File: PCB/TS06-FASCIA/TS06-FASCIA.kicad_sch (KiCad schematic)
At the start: 0 parts

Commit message: Add TS06 symbol library and the TS06-FASCIA schematic
tools/mksch.py generates both. 14 parts: SW1 rotary, SW2/SW3 levers, SW4/SW5
buttons, R1-R5 (4.7k 1% A6 divider), R6-R8 (A7 lever ladder), J1 6-pin JST-XH.
Balanced-parens checked; nets verified by label count.

No power symbols. This board has no power source - every net leaves through J1 -
so +5V and GND are plain local labels. A power flag here would describe nothing.

The rotary symbol's six taps are pitched 12.7mm so they sit directly opposite
their ladder nodes and the divider reads as the physical thing it is, top to
bottom, 0V to 5V.

Sheet carries four notes so the reasoning survives without the spec open: the two
ADC tables, why the 100nF caps are deliberately NOT here (they belong at the main
board end), and the lug geometry that rules out board-mounting anything.

Project sym-lib-table and fp-lib-table registered so TS06: resolves on open.

Co-Authored-By: Claude Opus 5 <noreply@anthropic.com>
Claude-Session: https://claude.ai/code/session_01Wbajb7CU1SV8ZUPn3KkB8i
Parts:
- added J1: JST-XH 6, symbol TS06:Conn_JST_XH_6
- added R1, R2, R3, R4, R5: 4.7k 1%, symbol TS06:R
- added R6, R8: 10k, symbol TS06:R
- added R7: 20k, symbol TS06:R
- added SW1: SR25 6-pos, symbol TS06:SW_Rotary_6P1W
- added SW2: LEVER A, symbol TS06:SW_Lever_MT1
- added SW3: LEVER B, symbol TS06:SW_Lever_MT1
- added SW4: MINUS, symbol TS06:SW_Button_KMD1
- added SW5: PLUS, symbol TS06:SW_Button_KMD1
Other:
- note added: "A6: five 4.7k 1% across +5V/GND, wiper picks a node. 23.5k string, 213uA, worst source Z 5.64k (ADC wants <10k). Taps land on 0/1/2/3/4/5 V -> ADC 0/205/409/614/818/1023, worst gap 204 codes."
- note added: "A7: 10k pull-up, 20k and 10k to ground. Four states at ADC 1023 / 682 / 512 / 409, worst gap 103 codes."
- note added: "Every switch is panel-mount with solder lugs sitting >=11.3mm BEHIND this board, pointing away. Nothing here is board-mounted; all are hand-wired to landing pads. Pole 2 of the rotary is spare and unwired."
- note added: "Five controls, six wires. The ladder is why."
- note added: "NOT on this board: the two 100nF filter caps. They go at the MAIN BOARD end of the cable, where they hold the last value if a non-shorting wiper floats and filter what the cable picks up passing a converter switching 185V at 31kHz."
- note added: "TS06-FASCIA - control panel and product face"

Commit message: Control scheme rev B: swap INFO to position 6, give SUB the glitch rate
Two changes to spec section 1, decided while designing the fascia face. Spec section
1 is not yet rewritten - this file is the authority until the sweep runs.

INFO and FORMAT/DATE swap. Section 1 already called positions 1 and 5 the two screens
that ignore every input; rev A left one of them mid-arc. Rev B puts both parking
screens on end stops, so the knob cannot be knocked past either end into a live
editing screen. Costs one row of the A6 threshold table - the voltages do not move,
only the screen each maps to.

SUB gains the glitch rate on Display, read only while FIELD = Effects. The point is
not the feature but that SUB now obeys a rule instead of an exception: it is read
only when FIELD is thrown to its second position, true on both screens that use it.
A rule can be learned once; an exception has to be printed.

Co-Authored-By: Claude Opus 5 <noreply@anthropic.com>
Claude-Session: https://claude.ai/code/session_01Wbajb7CU1SV8ZUPn3KkB8i
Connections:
- net +5V: now also J1.2 (+5V), R5.1, R6.1, SW1.6 (T6)
- net A6: now also J1.3 (A6), SW1.7 (COM)
- net A7: now also J1.4 (A7), R6.2, SW2.2 (B), SW3.2 (B)
- net D7: now also J1.5 (D7), SW4.2
- net D8: now also J1.6 (D8), SW5.2
- net GND: now also J1.1 (GND), R1.2, R7.2, R8.2, SW1.1 (T1), SW4.1, SW5.1
- new net: R8.1, SW3.1 (A)
- new net: R7.1, SW2.1 (A)
- new net: R1.1, R2.2, SW1.2 (T2)
- new net: R2.1, R3.2, SW1.3 (T3)
- new net: R3.1, R4.2, SW1.4 (T4)
- new net: R4.1, R5.2, SW1.5 (T5)
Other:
- company: (none) -> TERMINAL-06
- title: (none) -> TS06-FASCIA - control panel and product face
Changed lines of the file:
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@@
 (generator_version "10.0")
 (paper "A4")
+(title_block
+(title "TS06-FASCIA - control panel and product face")
+(date "2026-09-08")
+(rev "A")
+(company "TERMINAL-06")
+(comment 1 "Five controls, six wires. Generated by tools/mksch.py")
+(comment 2 "Dimensions from the calipered FreeCAD models in 3d/")
+)
 (symbol
 (lib_id "TS06:SW_Rotary_6P1W")
@@
 (pts
 (xy 139.7 107.95)
-(xy 139.7 114.3)
-)
-(stroke
-(width 0)
-(type default)
-)
-)
-(wire
-(pts
-(xy 139.7 121.92)
+(xy 139.7 110.49)
+)
+(stroke
+(width 0)
+(type default)
+)
+)
+(wire
+(pts
+(xy 139.7 125.73)
 (xy 139.7 127.0)
 )
@@
 (pts
 (xy 165.1 107.95)
-(xy 165.1 114.3)
-)
-(stroke
-(width 0)
-(type default)
-)
-)
-(wire
-(pts
-(xy 165.1 121.92)
+(xy 165.1 110.49)
+)
+(stroke
+(width 0)
+(type default)
+)
+)
+(wire
+(pts
+(xy 165.1 125.73)
 (xy 165.1 127.0)
 )
@@
 (symbol
 (lib_id "TS06:Conn_JST_XH_6")
-(at 261.62 80.01 0)
+(at 238.76 80.01 0)
 (unit 1)
 (exclude_from_sim no)
@@
 (fields_autoplaced yes)
 (property "Reference" "J1"
-(at 265.43 78.74000000000001 0)
+(at 242.57 78.74000000000001 0)
 (effects
 (font
@@
 )
 (property "Value" "JST-XH 6"
-(at 265.43 81.28 0)
+(at 242.57 81.28 0)
 (effects
 (font
@@
 (wire
 (pts
-(xy 269.24 78.74)
-(xy 279.4 78.74)
+(xy 246.38 81.28)
+(xy 256.53999999999996 81.28)
 )
 (stroke
@@
 )
 (label "GND"
-(at 279.4 78.74 0)
-(fields_autoplaced yes)
-(effects
-(font
-(size 1.27 1.27)
-)
-(justify left bottom)
-)
-)
-(wire
-(pts
-(xy 269.24 81.28)
-(xy 279.4 81.28)
+(at 256.53999999999996 81.28 0)
+(fields_autoplaced yes)
+(effects
+(font
+(size 1.27 1.27)
+)
+(justify left bottom)
+)
+)
+(wire
+(pts
+(xy 246.38 83.82000000000001)
+(xy 256.53999999999996 83.82000000000001)
 )
 (stroke
@@
 )
 (label "+5V"
-(at 279.4 81.28 0)
-(fields_autoplaced yes)
-(effects
-(font
-(size 1.27 1.27)
-)
-(justify left bottom)
-)
-)
-(wire
-(pts
-(xy 269.24 83.82)
-(xy 279.4 83.82)
+(at 256.53999999999996 83.82000000000001 0)
+(fields_autoplaced yes)
+(effects
+(font
+(size 1.27 1.27)
+)
+(justify left bottom)
+)
+)
+(wire
+(pts
+(xy 246.38 86.36)
+(xy 256.53999999999996 86.36)
 )
 (stroke
@@
 )
 (label "A6"
-(at 279.4 83.82 0)
-(fields_autoplaced yes)
-(effects
-(font
-(size 1.27 1.27)
-)
-(justify left bottom)
-)
-)
-(wire
-(pts
-(xy 269.24 86.36)
-(xy 279.4 86.36)
+(at 256.53999999999996 86.36 0)
+(fields_autoplaced yes)
+(effects
+(font
+(size 1.27 1.27)
+)
+(justify left bottom)
+)
+)
+(wire
+(pts
+(xy 246.38 88.9)
+(xy 256.53999999999996 88.9)
 )
 (stroke
@@
 )
 (label "A7"
-(at 279.4 86.36 0)
-(fields_autoplaced yes)
-(effects
-(font
-(size 1.27 1.27)
-)
-(justify left bottom)
-)
-)
-(wire
-(pts
-(xy 269.24 88.89999999999999)
-(xy 279.4 88.89999999999999)
+(at 256.53999999999996 88.9 0)
+(fields_autoplaced yes)
+(effects
+(font
+(size 1.27 1.27)
+)
+(justify left bottom)
+)
+)
+(wire
+(pts
+(xy 246.38 91.44)
+(xy 256.53999999999996 91.44)
 )
 (stroke
@@
 )
 (label "D7"
-(at 279.4 88.89999999999999 0)
-(fields_autoplaced yes)
-(effects
-(font
-(size 1.27 1.27)
-)
-(justify left bottom)
-)
-)
-(wire
-(pts
-(xy 269.24 91.44)
-(xy 279.4 91.44)
+(at 256.53999999999996 91.44 0)
+(fields_autoplaced yes)
+(effects
+(font
+(size 1.27 1.27)
+)
+(justify left bottom)
+)
+)
+(wire
+(pts
+(xy 246.38 93.98)
+(xy 256.53999999999996 93.98)
 )
 (stroke
@@
 )
 (label "D8"
-(at 279.4 91.44 0)
-(fields_autoplaced yes)
-(effects
+(at 256.53999999999996 93.98 0)
+(fields_autoplaced yes)
+(effects

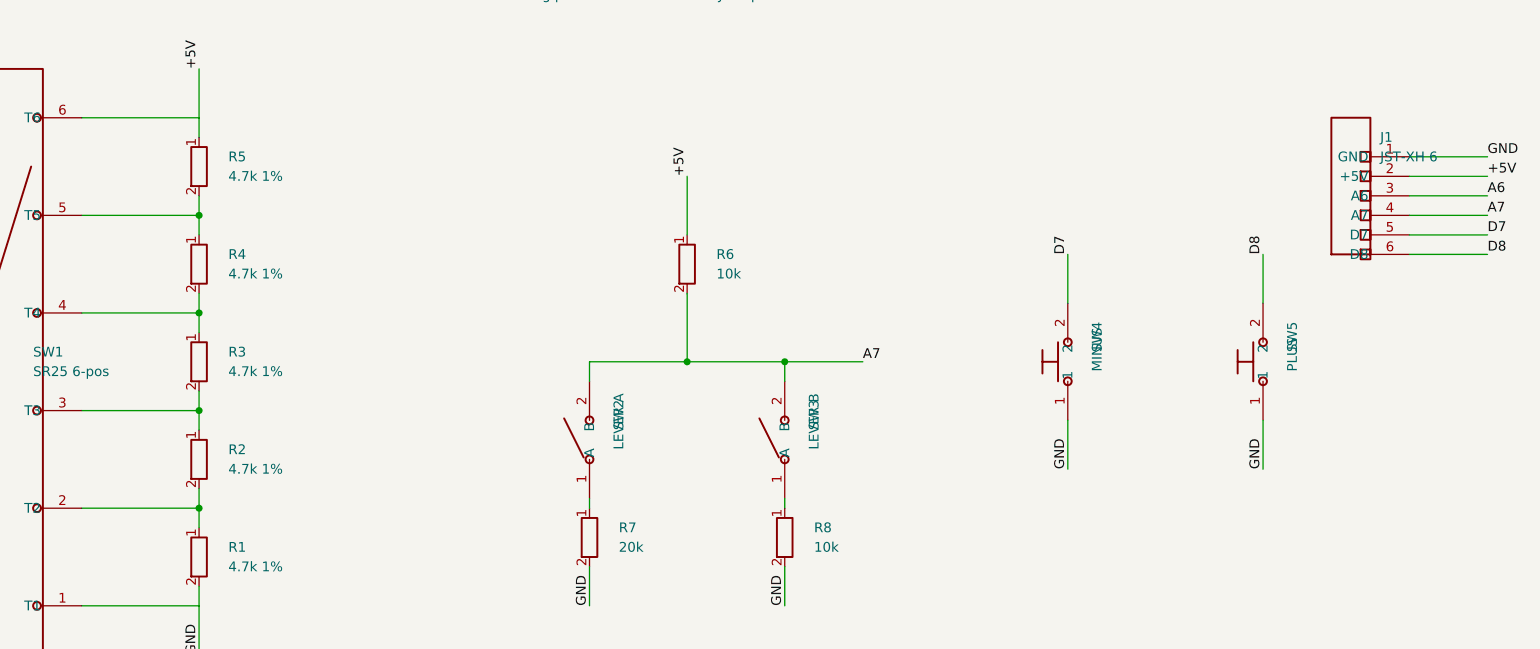
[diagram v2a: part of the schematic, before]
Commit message: Route TS06-FASCIA on two layers; link the schematic to the board
43 tracks, 7 vias, both clearance and connectivity checks clean at 0.2mm.

TWO LAYERS, deliberately. The front of this board is copper too, and a trace there is
invisible: solder mask is opaque, so only the deliberate mask openings show gold. That
makes F.Cu a free routing layer for anything clear of the decorative copper. All seven
vias are tented and sit at y > 45, in the band the chassis recess covers. Single-layer
was attempted first and does not fit: the switch body keepouts occupy everything above
y=38, leaving a 13mm band that already holds the landing pads, both resistor rows and
the connector - four buses through that means clearances under 0.5mm.

  B.Cu  the ladder, every local hop, the GND bus along the bottom edge, and A7
  F.Cu  the two long hauls, +5V at y=50 and A6 at y=47.2

J1's pin order is now chosen by the PCB rather than by tidiness - D8, D7, GND, A7,
+5V, A6 - so each net lands on the pin nearest the direction it arrives from and no
two traces cross to reach the connector. The schematic was regenerated to match.

Two crossings the checker caught and I fixed: both button grounds sat inside A7's lane
and could not drop straight to the bus, so they now collect above the button pads and
come down the right-hand edge. LEVB has the same problem and hops to the front for
2.3mm, landing inside the SUB box outline where the front is empty copper anyway.

New tool: tools/checkcopper.py - track/pad, track/track, via clearance per layer, plus
two things a naive checker misses. The decorative gold is NETLESS COPPER, so a routed
trace touching it is a short rather than an overlap; and gr_text on F.Cu is copper too,
so the dial numerals and the +/- glyphs get bounding boxes. Both are now checked.

Also fixed in tools/checksch.py: labels dropped on the MIDDLE of a wire were ignored,
which made correctly-named nets report as unnamed. KiCad attaches them; now so does the
checker.

The two files no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
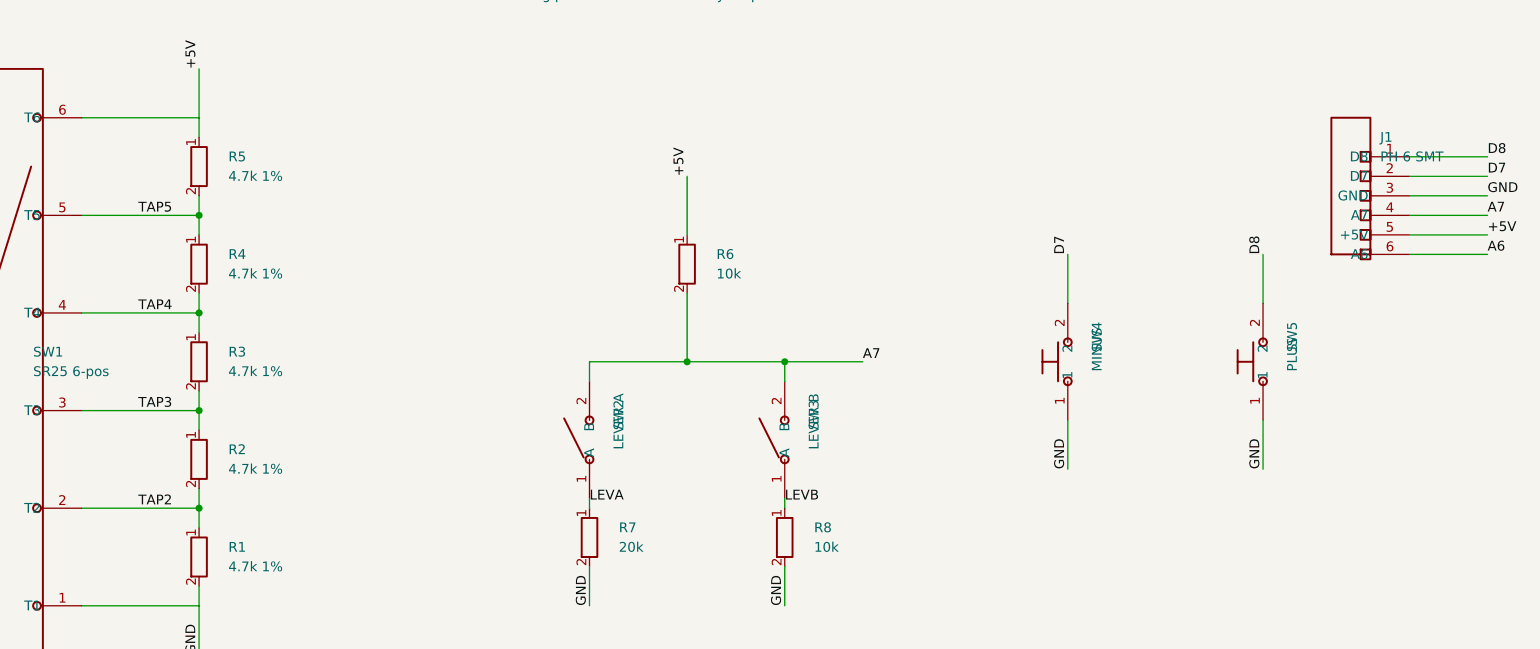
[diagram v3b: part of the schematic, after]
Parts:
- J1: value JST-XH 6 -> PH 6 SMT; footprint (none) -> TS06:TS06_JST_PH_S6B-PH-SM4-TB_Back
- R1, R2, R3, R4, R5, R6, R7, R8: footprint (none) -> TS06:TS06_R_1206_HandSolder
- SW1: footprint (none) -> TS06:TS06_Rotary_SR25_PanelMount
- SW2, SW3: footprint (none) -> TS06:TS06_MT1_Lever_PanelMount
- SW4, SW5: footprint (none) -> TS06:TS06_KMD1_Button_PanelMount
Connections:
- net +5V: now also J1.5 (+5V); no longer J1.2 (+5V)
- net A6: now also J1.6 (A6); no longer J1.3 (A6)
- net D7: now also J1.2 (D7); no longer J1.5 (D7)
- net D8: now also J1.1 (D8); no longer J1.6 (D8)
- net GND: now also J1.3 (GND); no longer J1.1 (GND)
- net LEVB: now reaches R8.1, SW3.1 (A)
- net LEVA: now reaches R7.1, SW2.1 (A)
- net TAP2: now reaches R1.1, R2.2, SW1.2 (T2)
- net TAP3: now reaches R2.1, R3.2, SW1.3 (T3)
- net TAP4: now reaches R3.1, R4.2, SW1.4 (T4)
- net TAP5: now reaches R4.1, R5.2, SW1.5 (T5)
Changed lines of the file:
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@@
+)
+)
+(property "Footprint" "TS06:TS06_Rotary_SR25_PanelMount"
+(at 63.5 107.95 0)
+(effects
+(font
+(size 1.27 1.27)
+)
+(hide yes)
 )
 )
@@
 )
 )
+(property "Footprint" "TS06:TS06_R_1206_HandSolder"
+(at 88.9 133.35 0)
+(effects
+(font
+(size 1.27 1.27)
+)
+(hide yes)
+)
+)
 (pin "1"
 )
@@
 )
 )
+(property "Footprint" "TS06:TS06_R_1206_HandSolder"
+(at 88.9 120.65 0)
+(effects
+(font
+(size 1.27 1.27)
+)
+(hide yes)
+)
+)
 (pin "1"
 )
@@
 )
 )
+(property "Footprint" "TS06:TS06_R_1206_HandSolder"
+(at 88.9 107.94999999999999 0)
+(effects
+(font
+(size 1.27 1.27)
+)
+(hide yes)
+)
+)
 (pin "1"
 )
@@
 )
 )
+(property "Footprint" "TS06:TS06_R_1206_HandSolder"
+(at 88.9 95.25 0)
+(effects
+(font
+(size 1.27 1.27)
+)
+(hide yes)
+)
+)
 (pin "1"
 )
@@
 )
 )
+(property "Footprint" "TS06:TS06_R_1206_HandSolder"
+(at 88.9 82.55000000000001 0)
+(effects
+(font
+(size 1.27 1.27)
+)
+(hide yes)
+)
+)
 (pin "1"
 )
@@
 )
 )
+(label "TAP2"
+(at 81.0 127.0 0)
+(fields_autoplaced yes)
+(effects
+(font
+(size 1.27 1.27)
+)
+(justify left bottom)
+)
+)
+(label "TAP3"
+(at 81.0 114.3 0)
+(fields_autoplaced yes)
+(effects
+(font
+(size 1.27 1.27)
+)
+(justify left bottom)
+)
+)
+(label "TAP4"
+(at 81.0 101.6 0)
+(fields_autoplaced yes)
+(effects
+(font
+(size 1.27 1.27)
+)
+(justify left bottom)
+)
+)
+(label "TAP5"
+(at 81.0 88.9 0)
+(fields_autoplaced yes)
+(effects
+(font
+(size 1.27 1.27)
+)
+(justify left bottom)
+)
+)
 (wire
 (pts
@@
 )
 )
+(property "Footprint" "TS06:TS06_R_1206_HandSolder"
+(at 152.4 95.25 0)
+(effects
+(font
+(size 1.27 1.27)
+)
+(hide yes)
+)
+)
 (pin "1"
 )
@@
 )
 )
+(property "Footprint" "TS06:TS06_MT1_Lever_PanelMount"
+(at 139.7 118.11 0)
+(effects
+(font
+(size 1.27 1.27)
+)
+(hide yes)
+)
+)
 (pin "1"
 )
@@
 )
 )
+(property "Footprint" "TS06:TS06_R_1206_HandSolder"
+(at 139.7 130.81 0)
+(effects
+(font
+(size 1.27 1.27)
+)
+(hide yes)
+)
+)
 (pin "1"
 )
@@
 )
 )
+(label "LEVA"
+(at 139.7 126.36500000000001 0)
+(fields_autoplaced yes)
+(effects
+(font
+(size 1.27 1.27)
+)
+(justify left bottom)
+)
+)
 (wire
 (pts
@@
 )
 )
+(property "Footprint" "TS06:TS06_MT1_Lever_PanelMount"
+(at 165.1 118.11 0)
+(effects
+(font
+(size 1.27 1.27)
+)
+(hide yes)
+)
+)
 (pin "1"
 )
@@
 )
 )
+(property "Footprint" "TS06:TS06_R_1206_HandSolder"
+(at 165.1 130.81 0)
+(effects
+(font
+(size 1.27 1.27)
+)
+(hide yes)
+)
+)
 (pin "1"
 )
@@
 )
 )
+(label "LEVB"
+(at 165.1 126.36500000000001 0)
+(fields_autoplaced yes)
+(effects
+(font
+(size 1.27 1.27)
+)
+(justify left bottom)
+)
+)
 (wire
 (pts
@@
 )
 )
+(property "Footprint" "TS06:TS06_KMD1_Button_PanelMount"
+(at 201.93 107.95 0)
+(effects
+(font
+(size 1.27 1.27)
+)
+(hide yes)
+)
+)
 (pin "1"
 )
@@
 )
 )
+(property "Footprint" "TS06:TS06_KMD1_Button_PanelMount"
+(at 227.33 107.95 0)
+(effects
+(font
+(size 1.27 1.27)
+)
+(hide yes)
+)
+)
 (pin "1"
 )
@@
 )
 )
-(property "Value" "JST-XH 6"
+(property "Value" "PH 6 SMT"
 (at 242.57 81.28 0)
 (effects
@@
 )
 (justify left)
+)
+)
+(property "Footprint" "TS06:TS06_JST_PH_S6B-PH-SM4-TB_Back"
+(at 238.76 80.01 0)
+(effects
+(font
+(size 1.27 1.27)
+)
+(hide yes)
 )
 )
@@
 )
 )
-(label "GND"
+(label "D8"
 (at 256.53999999999996 81.28 0)
 (fields_autoplaced yes)
@@
 )
 )
-(label "+5V"
+(label "D7"
 (at 256.53999999999996 83.82000000000001 0)
 (fields_autoplaced yes)
@@
 )
 )
-(label "A6"
+(label "GND"
 (at 256.53999999999996 86.36 0)
 (fields_autoplaced yes)
@@
 )
 )
-(label "D7"
+(label "+5V"
 (at 256.53999999999996 91.44 0)
 (fields_autoplaced yes)
@@
 )
 )
-(label "D8"
+(label "A6"
 (at 256.53999999999996 93.98 0)
 (fields_autoplaced yes)
